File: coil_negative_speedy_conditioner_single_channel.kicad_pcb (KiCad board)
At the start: 2 copper layers, 22.7 x 19.6 mm, 8 parts, among them J1 Conn_02x04_Counter_Clockwise, U1 4N25

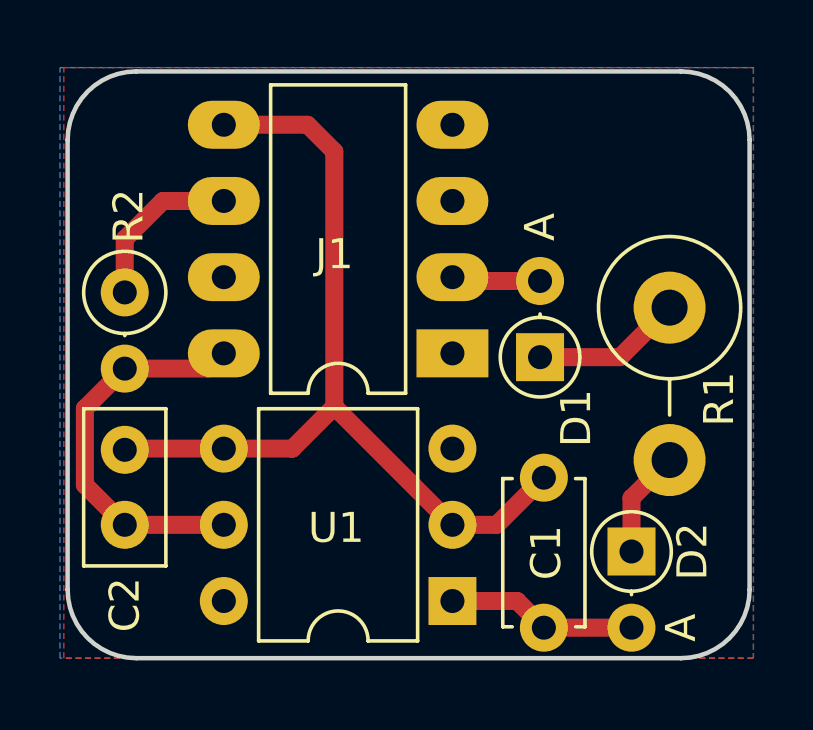
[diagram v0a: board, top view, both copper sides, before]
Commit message: VCC and GND flipped around
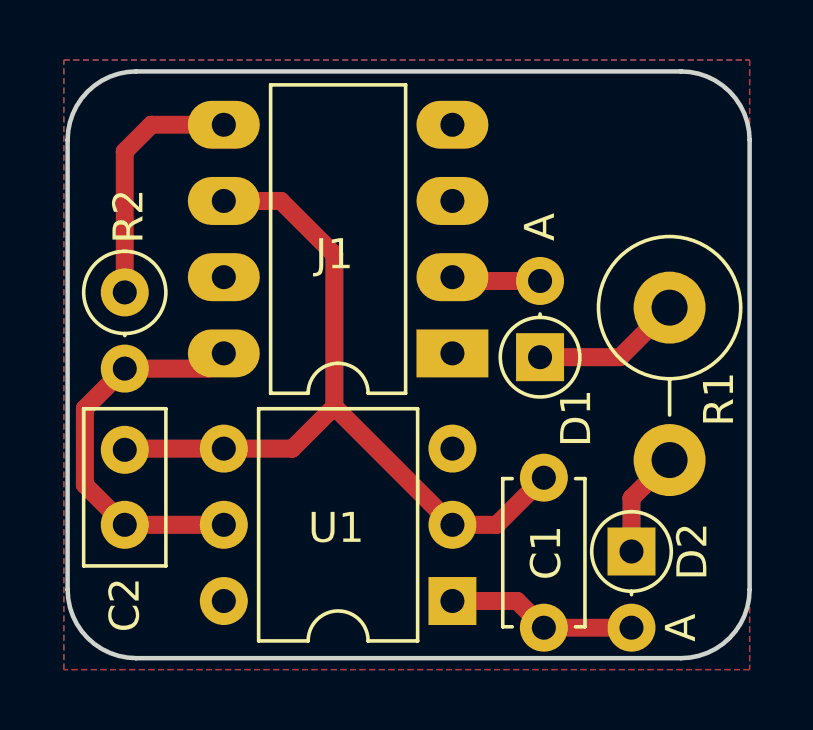
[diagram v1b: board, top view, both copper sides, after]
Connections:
- J1 pad 5: GND -> +5V
- J1 pad 6: +5V -> GND
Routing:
- net GND: track 29.4 -> 26.3 mm
- net +5V: track 5.61 -> 8.37 mm
